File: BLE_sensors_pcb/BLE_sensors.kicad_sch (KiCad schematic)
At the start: 1 part, among them U1 BME280

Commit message: Added lsm303
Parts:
- added U2: LSM303AHTR, My_Libraries:LSM303AHTR, symbol My_Libraries:LSM303AHTR
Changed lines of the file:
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@@
 	(paper "A4")
+	(symbol
+		(lib_id "My_Libraries:LSM303AHTR")
+		(at 137.16 102.87 0)
+		(unit 1)
+		(exclude_from_sim no)
+		(in_bom yes)
+		(on_board yes)
+		(dnp no)
+		(fields_autoplaced yes)
+		(property "Reference" "U2"
+			(at 172.72 92.71 0)
+			(effects
+				(font
+					(size 1.524 1.524)
+				)
+			)
+		)
+		(property "Value" "LSM303AHTR"
+			(at 172.72 95.25 0)
+			(effects
+				(font
+					(size 1.524 1.524)
+				)
+			)
+		)
+		(property "Footprint" "My_Libraries:LSM303AHTR"
+			(at 137.16 102.87 0)
+			(effects
+				(font
+					(size 1.27 1.27)
+					(italic yes)
+				)
+				(hide yes)
+			)
+		)
+		(property "Datasheet" "LSM303AHTR"
+			(at 137.16 102.87 0)
+			(effects
+				(font
+					(size 1.27 1.27)
+					(italic yes)
+				)
+				(hide yes)
+			)
+		)
+		(property "Description" ""
+			(at 137.16 102.87 0)
+			(effects
+				(font
+					(size 1.27 1.27)
+				)
+				(hide yes)
+			)
+		)
+		(pin "1"
+		)
+		(pin "11"
+		)
+		(pin "5"
+		)
+		(pin "3"
+		)
+		(pin "4"
+		)
+		(pin "6"
+		)
+		(pin "2"
+		)
+		(pin "12"
+		)
+		(pin "8"
+		)
+		(pin "7"
+		)
+		(pin "10"
+		)
+		(pin "9"
+		)
+		(instances
+			(project ""
+				(path "/06b47d3c-6b7b-411b-8755-cae193722202"
+					(reference "U2")
+					(unit 1)
+				)
+			)
+		)
+	)
 	(symbol
 		(lib_id "Sensor:BME280")

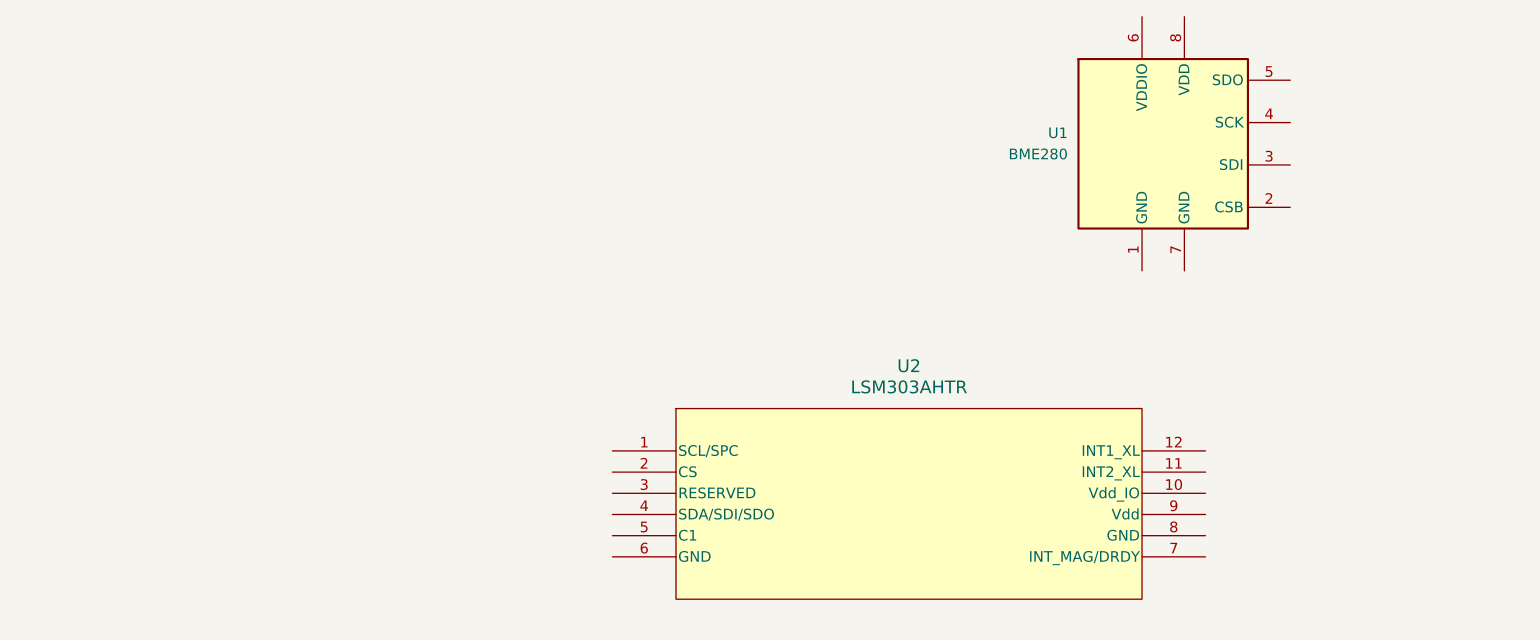
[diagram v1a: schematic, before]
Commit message: added BM15C
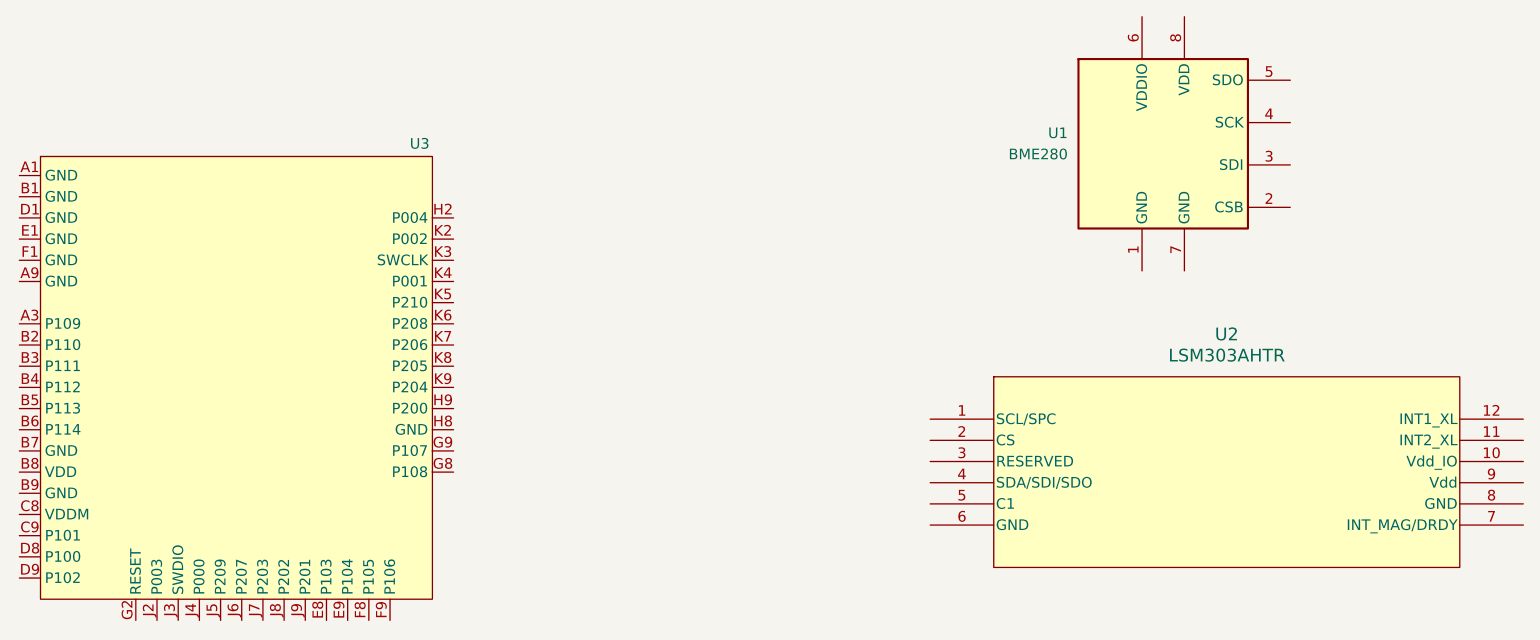
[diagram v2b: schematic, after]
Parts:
- added U3: ~, My_Libraries:BM15C, symbol My_Libraries:BM15C
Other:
- moved on the sheet: U2
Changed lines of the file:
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@@
 	(paper "A4")
 	(symbol
+		(lib_id "My_Libraries:BM15C")
+		(at 91.44 93.98 0)
+		(unit 1)
+		(exclude_from_sim no)
+		(in_bom yes)
+		(on_board yes)
+		(dnp no)
+		(property "Reference" "U3"
+			(at 114.046 66.04 0)
+			(effects
+				(font
+					(size 1.27 1.27)
+				)
+			)
+		)
+		(property "Value" "~"
+			(at 92.075 66.04 0)
+			(effects
+				(font
+					(size 1.27 1.27)
+				)
+			)
+		)
+		(property "Footprint" "My_Libraries:BM15C"
+			(at 91.44 93.98 0)
+			(effects
+				(font
+					(size 1.27 1.27)
+				)
+				(hide yes)
+			)
+		)
+		(property "Datasheet" ""
+			(at 91.44 93.98 0)
+			(effects
+				(font
+					(size 1.27 1.27)
+				)
+				(hide yes)
+			)
+		)
+		(property "Description" ""
+			(at 91.44 93.98 0)
+			(effects
+				(font
+					(size 1.27 1.27)
+				)
+				(hide yes)
+			)
+		)
+		(pin "B6"
+		)
+		(pin "D1"
+		)
+		(pin "A9"
+		)
+		(pin "A3"
+		)
+		(pin "B2"
+		)
+		(pin "A1"
+		)
+		(pin "B3"
+		)
+		(pin "B4"
+		)
+		(pin "J7"
+		)
+		(pin "B1"
+		)
+		(pin "E1"
+		)
+		(pin "F1"
+		)
+		(pin "B5"
+		)
+		(pin "C8"
+		)
+		(pin "D8"
+		)
+		(pin "B7"
+		)
+		(pin "B8"
+		)
+		(pin "C9"
+		)
+		(pin "G2"
+		)
+		(pin "J2"
+		)
+		(pin "D9"
+		)
+		(pin "J4"
+		)
+		(pin "J5"
+		)
+		(pin "B9"
+		)
+		(pin "J3"
+		)
+		(pin "J6"
+		)
+		(pin "J9"
+		)
+		(pin "H8"
+		)
+		(pin "K6"
+		)
+		(pin "K9"
+		)
+		(pin "K4"
+		)
+		(pin "E8"
+		)
+		(pin "F9"
+		)
+		(pin "K8"
+		)
+		(pin "K2"
+		)
+		(pin "H9"
+		)
+		(pin "E9"
+		)
+		(pin "J8"
+		)
+		(pin "H2"
+		)
+		(pin "K5"
+		)
+		(pin "F8"
+		)
+		(pin "K3"
+		)
+		(pin "K7"
+		)
+		(pin "G8"
+		)
+		(pin "G9"
+		)
+		(instances
+			(project ""
+				(path "/06b47d3c-6b7b-411b-8755-cae193722202"
+					(reference "U3")
+					(unit 1)
+				)
+			)
+		)
+	)
+	(symbol
 		(lib_id "My_Libraries:LSM303AHTR")
-		(at 137.16 102.87 0)
+		(at 175.26 99.06 0)
 		(unit 1)
 		(exclude_from_sim no)
@@
 		(fields_autoplaced yes)
 		(property "Reference" "U2"
-			(at 172.72 92.71 0)
+			(at 210.82 88.9 0)
 			(effects
 				(font
@@
 		)
 		(property "Value" "LSM303AHTR"
-			(at 172.72 95.25 0)
+			(at 210.82 91.44 0)
 			(effects
 				(font
@@
 		)
 		(property "Footprint" "My_Libraries:LSM303AHTR"
-			(at 137.16 102.87 0)
+			(at 175.26 99.06 0)
 			(effects
 				(font
@@
 		)
 		(property "Datasheet" "LSM303AHTR"
-			(at 137.16 102.87 0)
+			(at 175.26 99.06 0)
 			(effects
 				(font
@@
 		)
 		(property "Description" ""
-			(at 137.16 102.87 0)
-			(effects
-				(font
+			(at 175.26 99.06 0)
+			(effects
+				(font

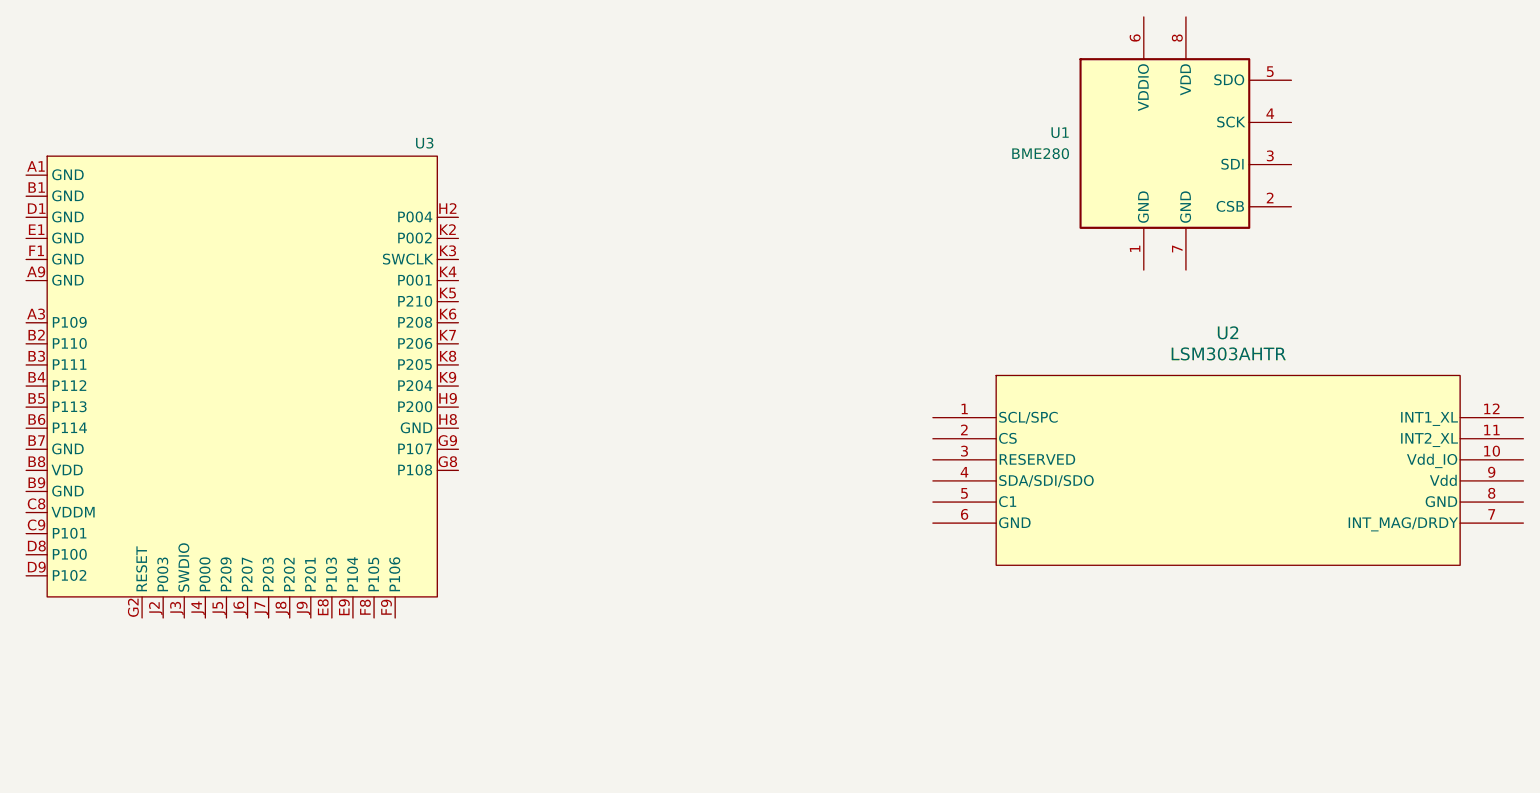
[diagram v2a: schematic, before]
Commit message: added datashet for me54bs01 and dev board and the me54bs01 to the kicad project
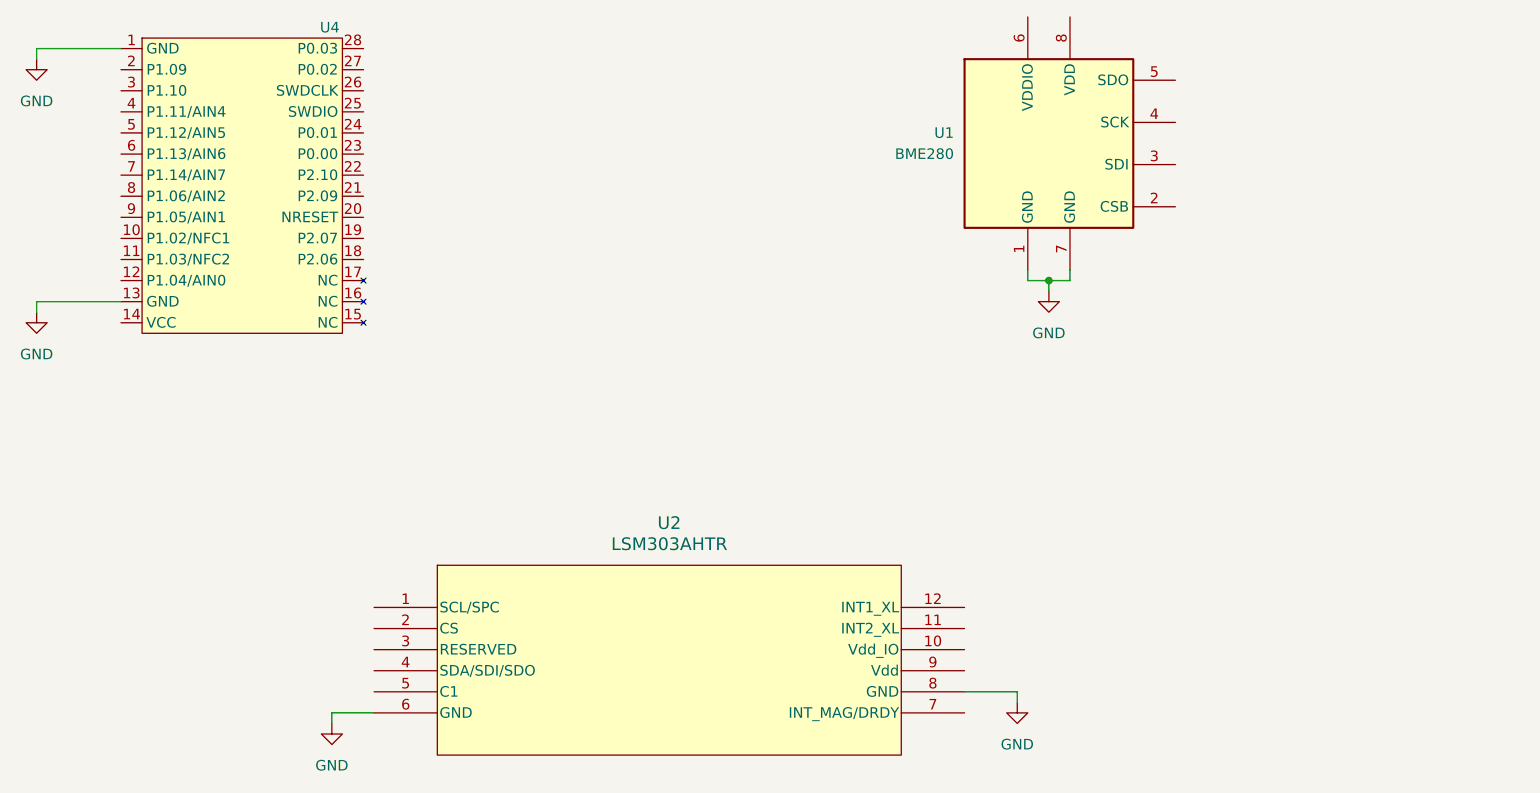
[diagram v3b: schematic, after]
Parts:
- removed U3: ~, My_Libraries:BM15C, symbol My_Libraries:BM15C
- added U4: ~, My_Libraries:Untitled, symbol My_Libraries:ME54BS01
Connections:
- net GND: now reaches U2.6 (GND)
- net GND: now also U1.1 (GND), U1.7 (GND), U2.8 (GND), U4.1 (GND), U4.13 (GND)
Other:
- moved on the sheet: U1, U2

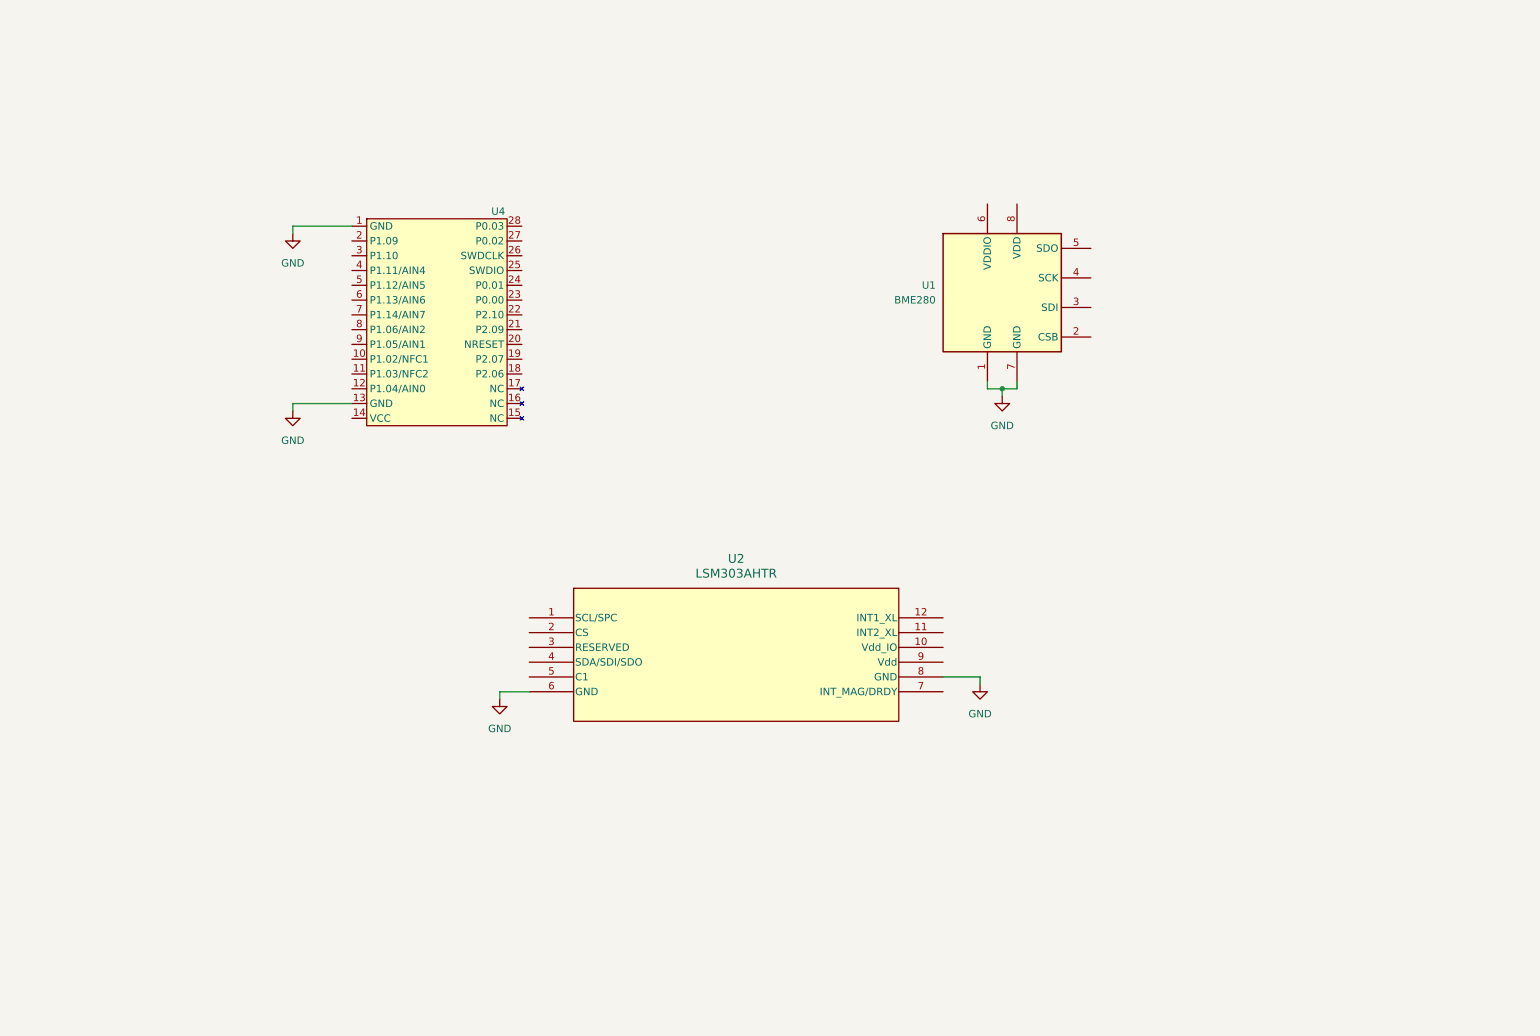
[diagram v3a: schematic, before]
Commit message: Refactor schematic and added power supplpy
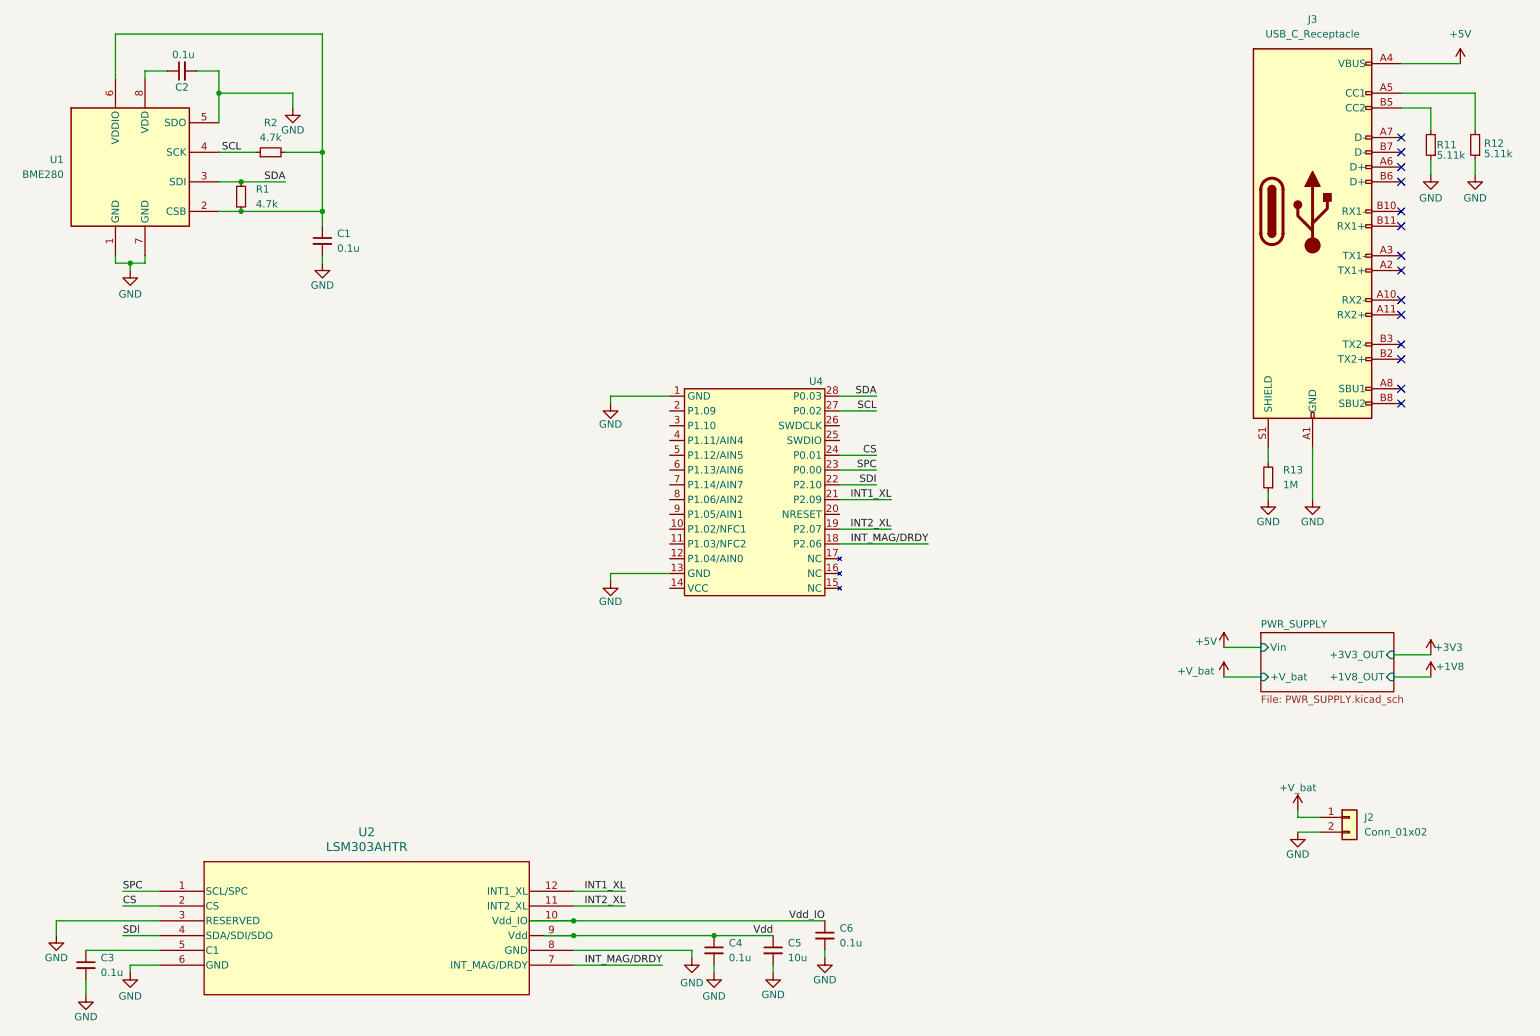
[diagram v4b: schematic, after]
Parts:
- added C1, C2, C3, C4, C6: 0.1u, symbol Device:C_Small
- added C5: 10u, symbol Device:C_Small
- added J2: Conn_01x02, symbol Connector_Generic:Conn_01x02
- added J3: USB_C_Receptacle, symbol Connector:USB_C_Receptacle
- added R1, R2: 4.7k, symbol Device:R_Small
- added R11, R12: 5.11k, symbol Device:R_Small
- added R13: 1M, symbol Device:R_Small
- U4: footprint My_Libraries:Untitled -> My_Libraries:ME54BS01
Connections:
- net GND: now also U1.5 (SDO), U2.3 (RESERVED), C1.2, C2.2, C3.2, C4.2, C5.2, C6.2, J2.2 (Pin_2), J3.A1 (GND), J3.A12 (GND), J3.B1 (GND), J3.B12 (GND), R11.1, R12.1, R13.1
- net INT_MAG/DRDY: now reaches U4.18 (P2.06)
- net INT_MAG/DRDY: now also U2.7 (INT_MAG/DRDY)
- net INT2_XL: now reaches U4.19 (P2.07)
- net INT2_XL: now also U2.11 (INT2_XL)
- net INT1_XL: now reaches U4.21 (P2.09)
- net INT1_XL: now also U2.12 (INT1_XL)
- net SDI: now reaches U4.22 (P2.10)
- net SDI: now also U2.4 (SDA/SDI/SDO)
- net SPC: now reaches U4.23 (P0.00)
- net SPC: now also U2.1 (SCL/SPC)
- net CS: now reaches U4.24 (P0.01)
- net CS: now also U2.2 (CS)
- net SCL: now reaches U4.27 (P0.02)
- net SCL: now also U1.4 (SCK), R2.1
- net SDA: now reaches U4.28 (P0.03)
- net SDA: now also U1.3 (SDI), R1.1
- net Vdd_IO: now reaches U2.10 (Vdd_IO)
- net Vdd_IO: now also C6.1
- net at U2.5 (C1): now also C3.1
- net Vdd: now reaches U2.9 (Vdd)
- net Vdd: now also C4.1, C5.1
- net at U1.2 (CSB): now also U1.6 (VDDIO), C1.1, R1.2, R2.2
- net at U1.8 (VDD): now also C2.1
- new net: J3.A5 (CC1), R12.2
- new net: J3.B5 (CC2), R11.2
- new net: J3.S1 (SHIELD), R13.2
- new net +5V: J3.A4 (VBUS), J3.A9 (VBUS), J3.B4 (VBUS), J3.B9 (VBUS)
- new net +V_bat: J2.1 (Pin_1)
- no-connect marks 0 -> 14
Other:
- added sheet PWR_SUPPLY (PWR_SUPPLY.kicad_sch)
- moved on the sheet: U1, U2, U4
